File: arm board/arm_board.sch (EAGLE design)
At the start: 95 parts, among them IC1 OPAMP-DUALU, J1 APPPP45_PCB_HORIZ_RIGHT, J14 APPPP45_PCB_HORIZ_RIGHT, J15 APPPP45_PCB_HORIZ_RIGHT, J16 APPPP45_PCB_HORIZ_RIGHT, J17 APPPP45_PCB_HORIZ_RIGHT, J18 APPPP45_PCB_HORIZ_RIGHT, J19 ENCODER, J2 APPPP45_PCB_HORIZ_RIGHT, J20 ENCODER, J21 ENCODER, J22 ENCODER, J24 ENCODER, J3 APPPP45_PCB_HORIZ_RIGHT, Q1 Q_IRF7437SMD, U1 TIVA-1294, U3 MAX3232D

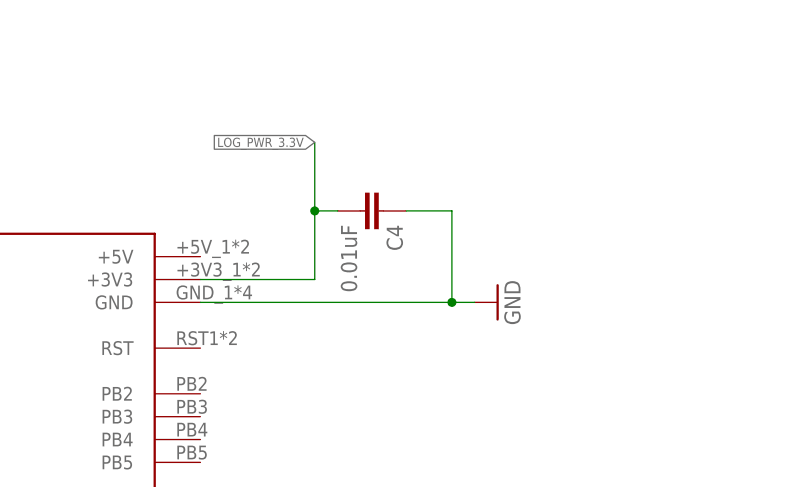
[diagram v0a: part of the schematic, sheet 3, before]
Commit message: added a power led
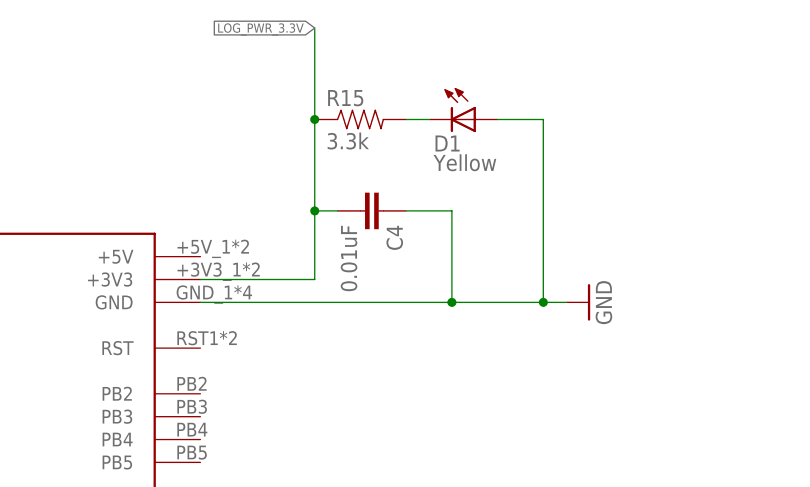
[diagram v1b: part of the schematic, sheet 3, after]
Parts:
- added D1: Yellow, SparkFun-LED:LED-YELLOWLILYPAD
- added R15: 3.3k, SparkFun-Resistors:8.2K-5%
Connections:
- new net N$16: D1.C, R15.2
- net GND: now also D1.A
- net LOG_PWR_3.3V: now also R15.1
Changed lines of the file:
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@@
 <part name="FRAME3" library="frames" deviceset="A3L-LOC" device=""/>
 <part name="FRAME4" library="frames" deviceset="A3L-LOC" device=""/>
+<part name="D1" library="SparkFun-LED" deviceset="LED-YELLOW" device="LILYPAD" value="Yellow"/>
+<part name="R15" library="SparkFun-Resistors" deviceset="8.2K-5%" device="" value="3.3k"/>
 </parts>
 <sheets>
@@
 <instances>
 <instance part="U1" gate="G$1" x="-7.62" y="7.62"/>
-<instance part="GND12" gate="1" x="55.88" y="116.84" rot="R90"/>
+<instance part="GND12" gate="1" x="66.04" y="116.84" rot="R90"/>
 <instance part="C4" gate="G$1" x="40.64" y="127" rot="R270"/>
 <instance part="U3" gate="G$1" x="127" y="76.2"/>
@@
 <instance part="GND15" gate="1" x="170.18" y="53.34"/>
 <instance part="FRAME3" gate="G$1" x="-99.06" y="-20.32"/>
+<instance part="D1" gate="G$1" x="53.34" y="137.16" rot="R270"/>
+<instance part="R15" gate="G$1" x="40.64" y="137.16"/>
 </instances>
 <busses>
@@
 <pinref part="GND12" gate="1" pin="GND"/>
 <pinref part="C4" gate="G$1" pin="1"/>
-<wire x1="50.8" y1="116.84" x2="53.34" y2="116.84" width="0.1524" layer="91"/>
+<wire x1="50.8" y1="116.84" x2="60.96" y2="116.84" width="0.1524" layer="91"/>
+<wire x1="60.96" y1="116.84" x2="63.5" y2="116.84" width="0.1524" layer="91"/>
 <wire x1="45.72" y1="127" x2="50.8" y2="127" width="0.1524" layer="91"/>
 <wire x1="50.8" y1="127" x2="50.8" y2="116.84" width="0.1524" layer="91"/>
 <junction x="50.8" y="116.84"/>
+<pinref part="D1" gate="G$1" pin="A"/>
+<wire x1="55.88" y1="137.16" x2="60.96" y2="137.16" width="0.1524" layer="91"/>
+<wire x1="60.96" y1="137.16" x2="60.96" y2="116.84" width="0.1524" layer="91"/>
+<junction x="60.96" y="116.84"/>
 </segment>
 <segment>
@@
 <net name="LOG_PWR_3.3V" class="0">
 <segment>
-<label x="35.56" y="134.62" size="1.016" layer="95" rot="R180" xref="yes"/>
+<label x="35.56" y="147.32" size="1.016" layer="95" rot="R180" xref="yes"/>
 <pinref part="U1" gate="G$1" pin="+3V3"/>
 <wire x1="22.86" y1="119.38" x2="35.56" y2="119.38" width="0.1524" layer="91"/>
-<wire x1="35.56" y1="134.62" x2="35.56" y2="127" width="0.1524" layer="91"/>
+<wire x1="35.56" y1="147.32" x2="35.56" y2="137.16" width="0.1524" layer="91"/>
 <pinref part="C4" gate="G$1" pin="2"/>
+<wire x1="35.56" y1="137.16" x2="35.56" y2="127" width="0.1524" layer="91"/>
 <wire x1="35.56" y1="127" x2="35.56" y2="119.38" width="0.1524" layer="91"/>
 <wire x1="38.1" y1="127" x2="35.56" y2="127" width="0.1524" layer="91"/>
 <junction x="35.56" y="127"/>
+<pinref part="R15" gate="G$1" pin="1"/>
+<junction x="35.56" y="137.16"/>
 </segment>
 <segment>
@@
 </segment>
 </net>
+<net name="N$16" class="0">
+<segment>
+<pinref part="R15" gate="G$1" pin="2"/>
+<pinref part="D1" gate="G$1" pin="C"/>
+<wire x1="45.72" y1="137.16" x2="48.26" y2="137.16" width="0.1524" layer="91"/>
+</segment>
+</net>

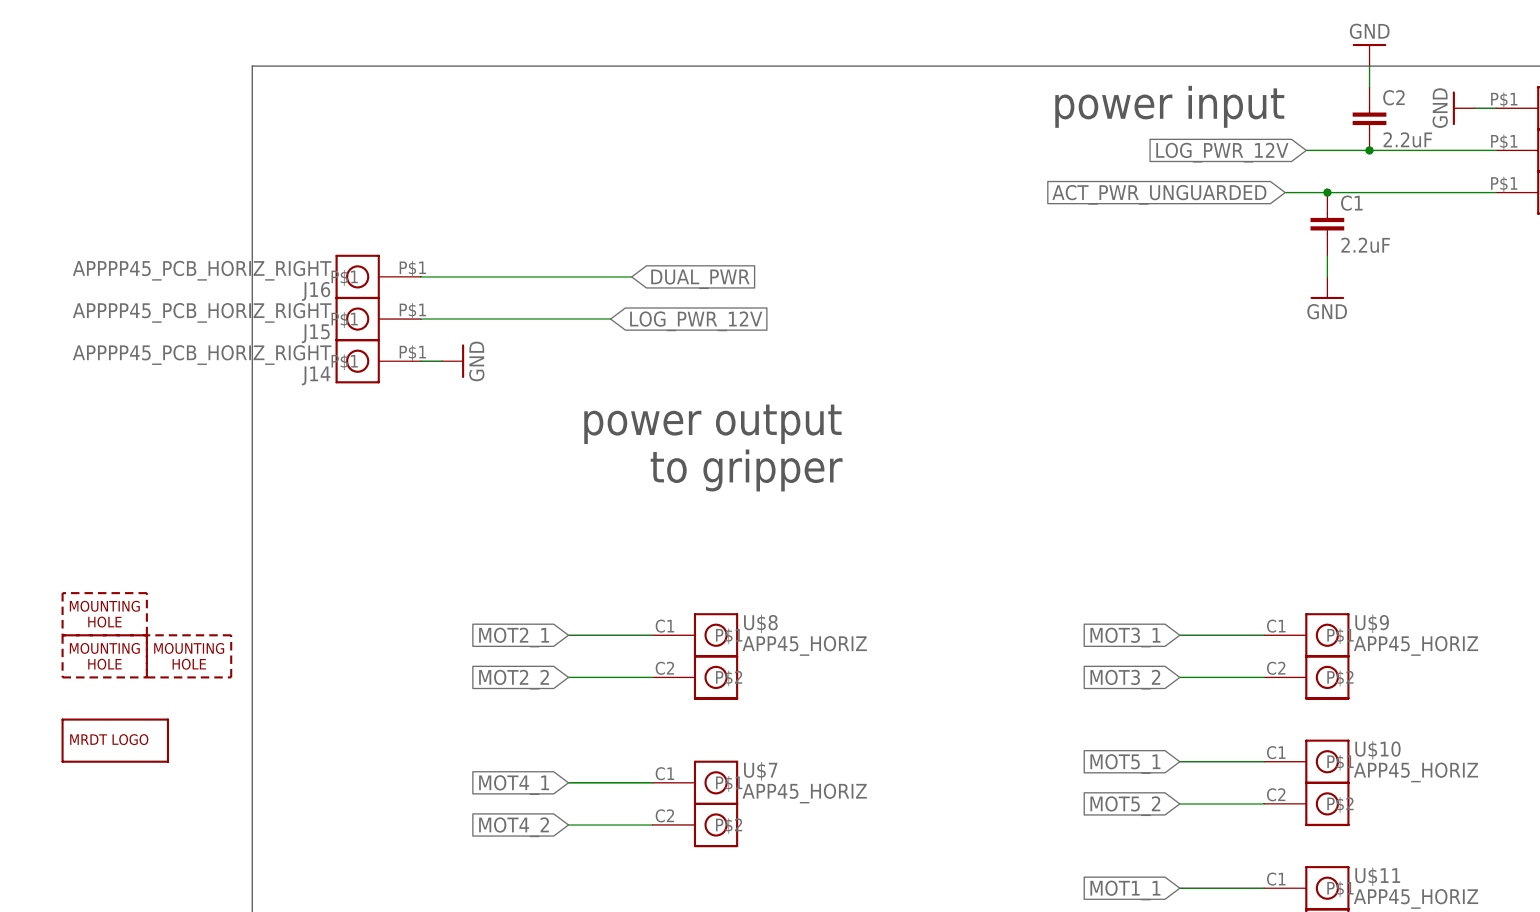
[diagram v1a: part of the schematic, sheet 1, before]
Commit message: components now use mrdt library
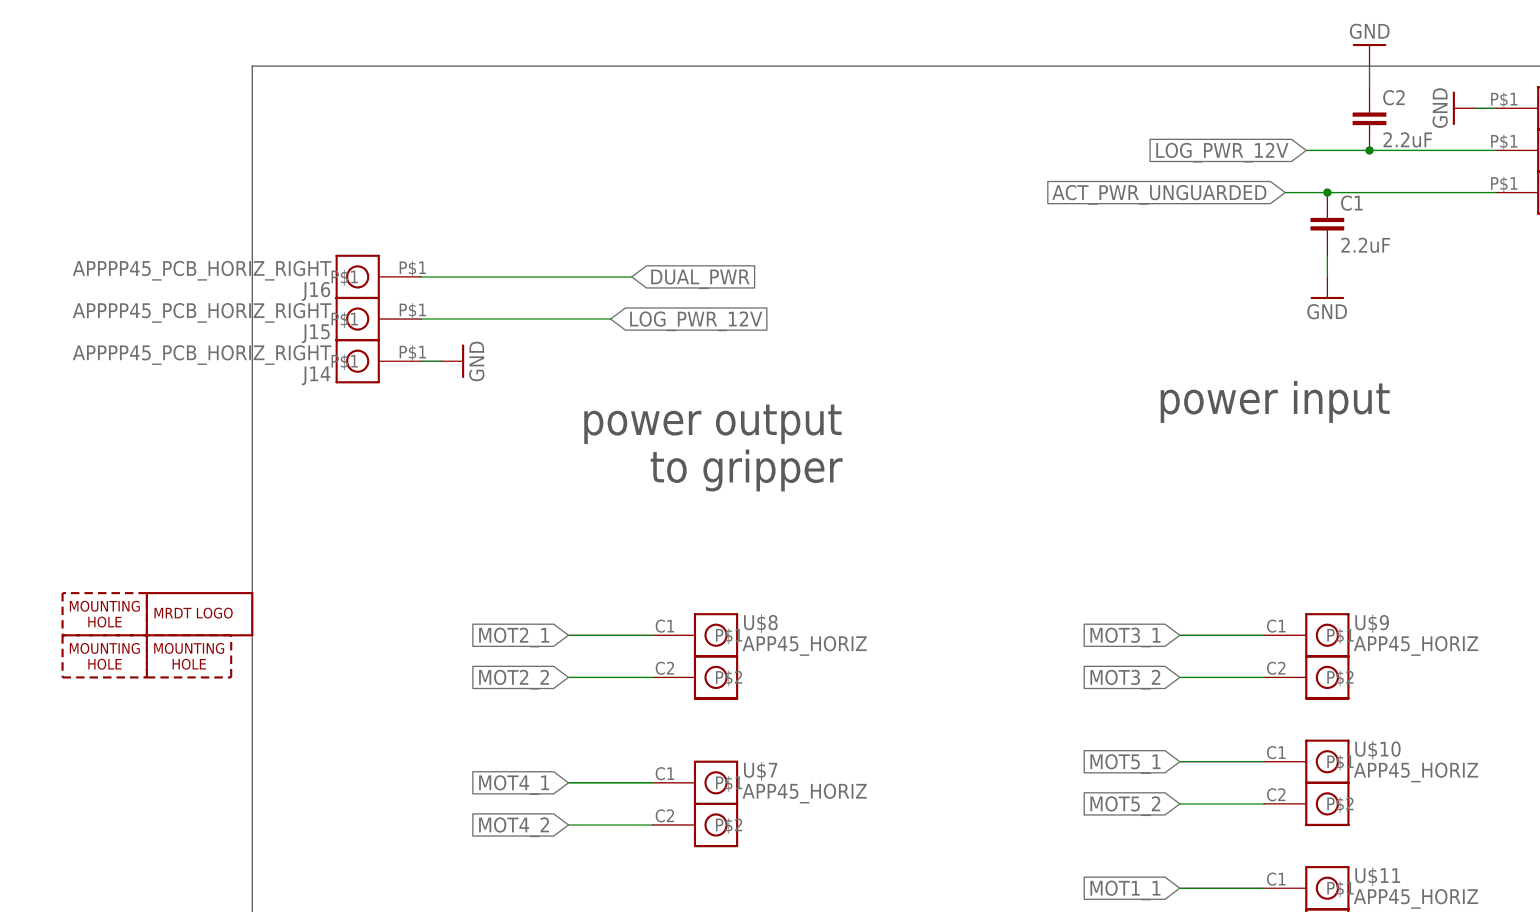
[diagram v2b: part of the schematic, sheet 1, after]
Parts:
- J19, J20, J21, J22, J24: device mine:ENCODER -> MRDT-Connectors:ENCODER
- MOT1_HB1, MOT2_HB1, MOT3_HB1, MOT5_HB1: device lin reg:DRV8829 -> MRDT-ICs:DRV8829
- MOT4_HB1: device mine:DRV8829 -> MRDT-ICs:DRV8829
- U$1: device lin reg:ACS722LL -> MRDT-ICs:ACS722LL
- U$2: device lin reg:MIC5219-3.3YM5 -> MRDT-ICs:MIC5219-3.3YM5
- U$4: device mine:SUD15N15 -> MRDT-Semiconductors:SUD15N15
- U$5, U$6: device mine:LM5050 -> MRDT-ICs:LM5050
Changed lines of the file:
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@@
 <part name="GND17" library="SparkFun-Aesthetics" deviceset="GND" device=""/>
 <part name="GND18" library="SparkFun-Aesthetics" deviceset="GND" device=""/>
-<part name="MOT2_HB1" library="lin reg" deviceset="DRV8829" device=""/>
+<part name="MOT2_HB1" library="MRDT-ICs" deviceset="DRV8829" device=""/>
 <part name="GND5" library="SparkFun-Aesthetics" deviceset="GND" device=""/>
 <part name="C31" library="SparkFun-Capacitors" deviceset="0.1UF-25V(+80/-20%)(0603)" device="" value=".47uF"/>
@@
 <part name="C35" library="SparkFun-Capacitors" deviceset="0.1UF-25V(+80/-20%)(0603)" device="" value=".01uF"/>
 <part name="GND9" library="SparkFun-Aesthetics" deviceset="GND" device=""/>
-<part name="MOT4_HB1" library="mine" deviceset="DRV8829" device=""/>
+<part name="MOT4_HB1" library="MRDT-ICs" deviceset="DRV8829" device=""/>
 <part name="GND44" library="SparkFun-Aesthetics" deviceset="GND" device=""/>
 <part name="C36" library="SparkFun-Capacitors" deviceset="0.1UF-25V(+80/-20%)(0603)" device="" value=".47uF"/>
@@
 <part name="C40" library="SparkFun-Capacitors" deviceset="0.1UF-25V(+80/-20%)(0603)" device="" value=".01uF"/>
 <part name="GND48" library="SparkFun-Aesthetics" deviceset="GND" device=""/>
-<part name="MOT3_HB1" library="lin reg" deviceset="DRV8829" device=""/>
+<part name="MOT3_HB1" library="MRDT-ICs" deviceset="DRV8829" device=""/>
 <part name="GND49" library="SparkFun-Aesthetics" deviceset="GND" device=""/>
 <part name="C41" library="SparkFun-Capacitors" deviceset="0.1UF-25V(+80/-20%)(0603)" device="" value=".47uF"/>
@@
 <part name="C45" library="SparkFun-Capacitors" deviceset="0.1UF-25V(+80/-20%)(0603)" device="" value=".01uF"/>
 <part name="GND53" library="SparkFun-Aesthetics" deviceset="GND" device=""/>
-<part name="MOT5_HB1" library="lin reg" deviceset="DRV8829" device=""/>
+<part name="MOT5_HB1" library="MRDT-ICs" deviceset="DRV8829" device=""/>
 <part name="GND54" library="SparkFun-Aesthetics" deviceset="GND" device=""/>
 <part name="C46" library="SparkFun-Capacitors" deviceset="0.1UF-25V(+80/-20%)(0603)" device="" value=".47uF"/>
@@
 <part name="C50" library="SparkFun-Capacitors" deviceset="0.1UF-25V(+80/-20%)(0603)" device="" value=".01uF"/>
 <part name="GND58" library="SparkFun-Aesthetics" deviceset="GND" device=""/>
-<part name="MOT1_HB1" library="lin reg" deviceset="DRV8829" device=""/>
+<part name="MOT1_HB1" library="MRDT-ICs" deviceset="DRV8829" device=""/>
 <part name="GND59" library="SparkFun-Aesthetics" deviceset="GND" device=""/>
 <part name="C51" library="SparkFun-Capacitors" deviceset="0.1UF-25V(+80/-20%)(0603)" device="" value=".47uF"/>
@@
 <part name="C55" library="SparkFun-Capacitors" deviceset="0.1UF-25V(+80/-20%)(0603)" device="" value=".01uF"/>
 <part name="GND63" library="SparkFun-Aesthetics" deviceset="GND" device=""/>
-<part name="U$2" library="lin reg" deviceset="MIC5219-3.3YM5" device=""/>
+<part name="U$2" library="MRDT-ICs" deviceset="MIC5219-3.3YM5" device=""/>
 <part name="GND19" library="SparkFun-Aesthetics" deviceset="GND" device=""/>
 <part name="C6" library="SparkFun-Capacitors" deviceset="1.0UF-16V-10%(0603)" device="" value="1.0uF"/>
@@
 <part name="C10" library="SparkFun-Capacitors" deviceset="1UF-25V-10%(0805)" device="" value="10uF"/>
 <part name="GND22" library="SparkFun-Aesthetics" deviceset="GND" device=""/>
-<part name="U$1" library="lin reg" deviceset="ACS722LL" device="" value="ACS722LLCTR-40AU"/>
+<part name="U$1" library="MRDT-ICs" deviceset="ACS722LL" device="" value="ACS722LLCTR-40AU"/>
 <part name="GND23" library="SparkFun-Aesthetics" deviceset="GND" device=""/>
 <part name="C9" library="SparkFun-Capacitors" deviceset="0.1UF-25V(+80/-20%)(0603)" device="" value="2.2uF"/>
@@
 <part name="LOGO1" library="MRDT-Hardware" deviceset="MRDT_LOGO" device=""/>
 <part name="U$3" library="mine" deviceset="SUD15N15" device=""/>
-<part name="U$4" library="mine" deviceset="SUD15N15" device=""/>
-<part name="U$5" library="mine" deviceset="LM5050" device=""/>
-<part name="U$6" library="mine" deviceset="LM5050" device=""/>
+<part name="U$4" library="MRDT-Semiconductors" deviceset="SUD15N15" device=""/>
+<part name="U$5" library="MRDT-ICs" deviceset="LM5050" device=""/>
+<part name="U$6" library="MRDT-ICs" deviceset="LM5050" device=""/>
 <part name="C12" library="SparkFun-Capacitors" deviceset="CAP_POL" device="C" value="330uF"/>
 <part name="C13" library="SparkFun-Capacitors" deviceset="CAP_POL" device="C" value="330uF"/>
@@
 <part name="R13" library="SparkFun-Passives" deviceset="RESISTOR" device="0603-RES" value="10k"/>
 <part name="R14" library="SparkFun-Passives" deviceset="RESISTOR" device="0603-RES" value="10k"/>
-<part name="J24" library="mine" deviceset="ENCODER" device=""/>
-<part name="J19" library="mine" deviceset="ENCODER" device=""/>
-<part name="J20" library="mine" deviceset="ENCODER" device=""/>
-<part name="J21" library="mine" deviceset="ENCODER" device=""/>
-<part name="J22" library="mine" deviceset="ENCODER" device=""/>
+<part name="J24" library="MRDT-Connectors" deviceset="ENCODER" device=""/>
+<part name="J19" library="MRDT-Connectors" deviceset="ENCODER" device=""/>
+<part name="J20" library="MRDT-Connectors" deviceset="ENCODER" device=""/>
+<part name="J21" library="MRDT-Connectors" deviceset="ENCODER" device=""/>
+<part name="J22" library="MRDT-Connectors" deviceset="ENCODER" device=""/>
 <part name="U$7" library="mine" deviceset="APP45_HORIZ" device=""/>
 <part name="U$8" library="mine" deviceset="APP45_HORIZ" device=""/>
@@
 <wire x1="119.38" y1="-43.18" x2="-78.74" y2="-43.18" width="0.1524" layer="97"/>
 <wire x1="-78.74" y1="-43.18" x2="-78.74" y2="127" width="0.1524" layer="97"/>
-<text x="45.72" y="124.46" size="3.81" layer="97" rot="R180">power input</text>
+<text x="58.42" y="88.9" size="3.81" layer="97" rot="R180">power input</text>
 <text x="-33.02" y="20.32" size="3.81" layer="97">motor I/O</text>
 <text x="-66.04" y="-27.94" size="3.81" layer="97">encoder I/O</text>
@@
 <instance part="H1" gate="G$1" x="-101.6" y="58.42"/>
 <instance part="H2" gate="G$1" x="-101.6" y="53.34"/>
-<instance part="LOGO1" gate="G$1" x="-101.6" y="43.18"/>
+<instance part="LOGO1" gate="G$1" x="-91.44" y="58.42"/>
 <instance part="J17" gate="G$1" x="104.14" y="99.06"/>
 <instance part="J18" gate="G$1" x="104.14" y="104.14"/>
